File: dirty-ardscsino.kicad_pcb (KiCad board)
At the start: 2 copper layers, 42.7 x 75.2 mm, 15 parts, among them J1 SCSI, J2 Ext. Power (Unused), J3 DM3AT-SF-PEJM5, U1 STM32 Bluepill

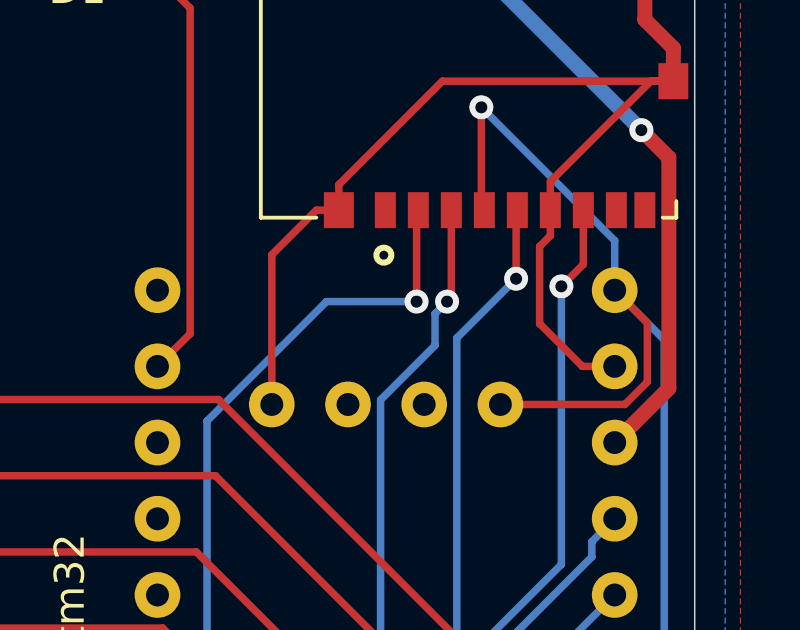
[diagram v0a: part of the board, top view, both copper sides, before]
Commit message: Delete programming header from bluepill footprint
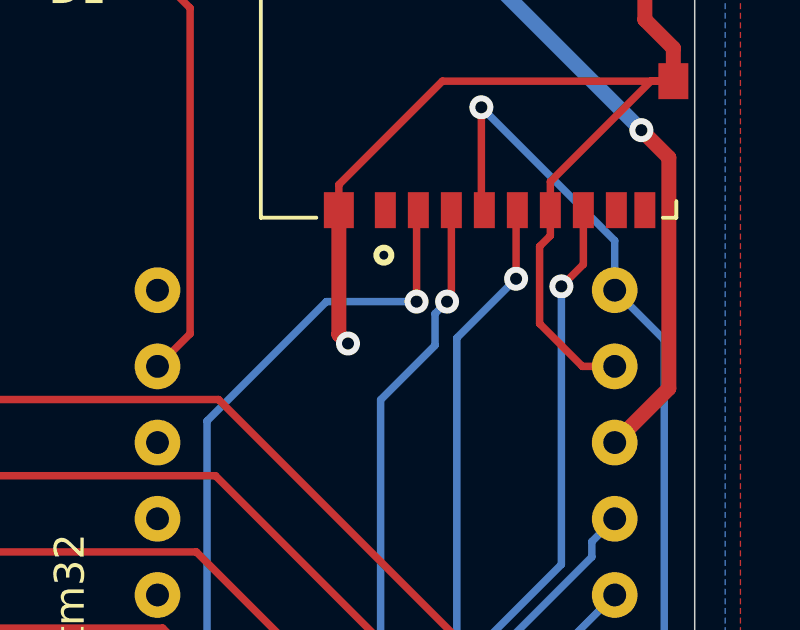
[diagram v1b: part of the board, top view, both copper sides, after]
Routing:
- net /SD_VCC: track 85.3 -> 76.6 mm
- net GND: track 88.5 -> 85.2 mm, vias 2 -> 3
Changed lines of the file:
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@@
     (thickness 1.6)
     (drawings 10)
-    (tracks 341)
+    (tracks 337)
     (zones 0)
     (modules 15)
-    (nets 50)
+    (nets 48)
   )
   (page A4)
@@
   (net 42 "Net-(U1-PadPC14)")
   (net 43 "Net-(U1-PadNRST)")
-  (net 44 "Net-(U1-PadPB2)")
-  (net 45 "Net-(U1-PadBOOT)")
-  (net 46 "Net-(J3-PadSWA)")
-  (net 47 "Net-(J3-PadSWB)")
-  (net 48 "Net-(J3-Pad8)")
-  (net 49 "Net-(J3-Pad1)")
+  (net 44 "Net-(J3-PadSWA)")
+  (net 45 "Net-(J3-PadSWB)")
+  (net 46 "Net-(J3-Pad8)")
+  (net 47 "Net-(J3-Pad1)")
   (net_class Default "This is the default net class."
     (clearance 0.2)
@@
     (add_net "Net-(R2-Pad2)")
     (add_net "Net-(R3-Pad2)")
-    (add_net "Net-(U1-PadBOOT)")
     (add_net "Net-(U1-PadNRST)")
     (add_net "Net-(U1-PadPA0)")
@@
     (add_net "Net-(U1-PadPA3)")
     (add_net "Net-(U1-PadPB1)")
-    (add_net "Net-(U1-PadPB2)")
     (add_net "Net-(U1-PadPC14)")
     (add_net "Net-(U1-PadPC15)")
@@
     (pad PB11 thru_hole circle (at 5.715 -10.795 180) (size 1.524 1.524) (drill 0.762) (layers *.Cu *.Mask)
       (net 21 /SCSI_DAT3))
-    (pad PB2 smd circle (at 2.54 27.305 180) (size 1.524 1.524) (layers Dwgs.User)
-      (net 44 "Net-(U1-PadPB2)"))
-    (pad BOOT smd circle (at 2.54 25.4 180) (size 1.524 1.524) (layers Dwgs.User)
-      (net 45 "Net-(U1-PadBOOT)"))
-    (pad 3V3 thru_hole circle (at -5.715 23.495 180) (size 1.524 1.524) (drill 0.762) (layers *.Cu *.Mask)
-      (net 3 /SD_VCC))
-    (pad SWO thru_hole circle (at -3.175 23.495 180) (size 1.524 1.524) (drill 0.762) (layers *.Cu *.Mask))
-    (pad SWCLK thru_hole circle (at -0.635 23.495 180) (size 1.524 1.524) (drill 0.762) (layers *.Cu *.Mask))
-    (pad G thru_hole circle (at 1.905 23.495 180) (size 1.524 1.524) (drill 0.762) (layers *.Cu *.Mask)
-      (net 2 GND))
   )
   (module Symbol:OSHW-Logo2_14.6x12mm_SilkScreen locked (layer B.Cu)
@@
       (effects (font (size 1 1) (thickness 0.15)))
     )
+    (fp_circle (center 0 0) (end 3.45 0) (layer F.CrtYd) (width 0.05))
+    (fp_circle (center 0 0) (end 3.2 0) (layer Cmts.User) (width 0.15))
     (fp_text user %R (at 0.3 0) (layer F.Fab)
       (effects (font (size 1 1) (thickness 0.15)))
     )
-    (fp_circle (center 0 0) (end 3.2 0) (layer Cmts.User) (width 0.15))
-    (fp_circle (center 0 0) (end 3.45 0) (layer F.CrtYd) (width 0.05))
     (pad 1 np_thru_hole circle (at 0 0) (size 3.2 3.2) (drill 3.2) (layers *.Cu *.Mask))
   )
@@
       (net 2 GND))
     (pad SWA smd rect (at -6.4 10.5 180) (size 1 0.8) (layers F.Cu F.Paste F.Mask)
-      (net 46 "Net-(J3-PadSWA)"))
+      (net 44 "Net-(J3-PadSWA)"))
     (pad P1 smd rect (at -6.4 4.3 180) (size 1 1.2) (layers F.Cu F.Paste F.Mask)
       (net 2 GND))
@@
       (net 2 GND))
     (pad SWB smd rect (at -5.45 0 180) (size 0.7 1.2) (layers F.Cu F.Paste F.Mask)
-      (net 47 "Net-(J3-PadSWB)"))
+      (net 45 "Net-(J3-PadSWB)"))
     (pad 8 smd rect (at -4.5 0 180) (size 0.7 1.2) (layers F.Cu F.Paste F.Mask)
-      (net 48 "Net-(J3-Pad8)"))
+      (net 46 "Net-(J3-Pad8)"))
     (pad 7 smd rect (at -3.4 0 180) (size 0.7 1.2) (layers F.Cu F.Paste F.Mask)
       (net 33 /SD_MISO))
@@
       (net 39 /SD_CS))
     (pad 1 smd rect (at 3.2 0 180) (size 0.7 1.2) (layers F.Cu F.Paste F.Mask)
-      (net 49 "Net-(J3-Pad1)"))
+      (net 47 "Net-(J3-Pad1)"))
   )
   (module Resistor_THT:R_Array_SIP10 (layer F.Cu)
@@
   (segment (start 175.922001 98.397999) (end 175.922001 90.705001) (width 0.5) (layer F.Cu) (net 1))
   (segment (start 175.922001 90.705001) (end 175.006 89.789) (width 0.5) (layer F.Cu) (net 1))
-  (segment (start 174.117 100.203) (end 175.922001 98.397999) (width 0.5) (layer F.Cu) (net 1))
-  (segment (start 163.195 77.978) (end 155.194 77.978) (width 0.5) (layer B.Cu) (net 1))
+  (segment (start 174.117 100.203) (end 175.922001 98.397999) (width 0.5) (layer F.Cu) (net 1) (status 10))
+  (segment (start 163.195 77.978) (end 155.194 77.978) (width 0.5) (layer B.Cu) (net 1) (status 20))
   (segment (start 175.006 89.789) (end 163.195 77.978) (width 0.5) (layer B.Cu) (net 1))
   (segment (start 163.022 77.806) (end 162.572 77.356) (width 0.5) (layer F.Cu) (net 2) (status 30))
@@
   (segment (start 146.304 89.154) (end 146.558 88.9) (width 0.5) (layer F.Cu) (net 2))
   (segment (start 146.304 90.914) (end 146.304 89.154) (width 0.5) (layer F.Cu) (net 2) (status 10))
-  (segment (start 164.172 92.456) (end 164.922 92.456) (width 0.25) (layer F.Cu) (net 2) (status 20))
-  (segment (start 162.687 93.941) (end 164.172 92.456) (width 0.25) (layer F.Cu) (net 2))
-  (segment (start 162.687 98.933) (end 162.687 93.941) (width 0.25) (layer F.Cu) (net 2) (status 10))
   (segment (start 157.79937 140.843) (end 158.877 140.843) (width 0.25) (layer B.Cu) (net 2) (status 20))
   (segment (start 157.506369 140.549999) (end 157.79937 140.843) (width 0.25) (layer B.Cu) (net 2))
@@
   (via (at 162.814 79.375) (size 0.8) (drill 0.4) (layers F.Cu B.Cu) (net 2))
   (segment (start 162.572 79.133) (end 162.814 79.375) (width 0.25) (layer F.Cu) (net 2))
-  (segment (start 162.572 77.356) (end 162.572 79.133) (width 0.25) (layer F.Cu) (net 2))
+  (segment (start 162.572 77.356) (end 162.572 79.133) (width 0.25) (layer F.Cu) (net 2) (status 10))
+  (via (at 165.227 96.901) (size 0.8) (drill 0.4) (layers F.Cu B.Cu) (net 2))
+  (segment (start 164.922 96.596) (end 165.227 96.901) (width 0.5) (layer F.Cu) (net 2))
+  (segment (start 164.922 92.456) (end 164.922 96.596) (width 0.5) (layer F.Cu) (net 2))
   (segment (start 174.638761 141.930001) (end 175.768 140.800762) (width 0.25) (layer B.Cu) (net 3))
   (segment (start 169.968238 138.303) (end 173.595239 141.930001) (width 0.25) (layer B.Cu) (net 3))
@@
   (segment (start 175.768 96.774) (end 174.117 95.123) (width 0.25) (layer B.Cu) (net 3) (status 20))
   (segment (start 175.768 140.800762) (end 175.768 96.774) (width 0.25) (layer B.Cu) (net 3))
-  (segment (start 175.204001 96.210001) (end 174.117 95.123) (width 0.25) (layer F.Cu) (net 3) (status 20))
-  (segment (start 175.204001 98.184761) (end 175.204001 96.210001) (width 0.25) (layer F.Cu) (net 3))
-  (segment (start 174.455762 98.933) (end 175.204001 98.184761) (width 0.25) (layer F.Cu) (net 3))
-  (segment (start 170.307 98.933) (end 174.455762 98.933) (width 0.25) (layer F.Cu) (net 3) (status 10))
   (segment (start 174.117 93.472) (end 169.672 89.027) (width 0.25) (layer B.Cu) (net 3))
   (via (at 169.672 89.027) (size 0.8) (drill 0.4) (layers F.Cu B.Cu) (net 3))
@@
   (segment (start 151.675999 103.848001) (end 160.171811 103.848001) (width 0.25) (layer F.Cu) (net 8))
   (segment (start 150.876 104.648) (end 151.675999 103.848001) (width 0.25) (layer F.Cu) (net 8) (status 10))
-  (segment (start 144.272 112.268) (end 150.876 112.268) (width 0.25) (layer F.Cu) (net 11) (status 30))
   (segment (start 144.272 107.188) (end 150.876 107.188) (width 0.25) (layer F.Cu) (net 9) (status 30))
   (segment (start 143.472001 106.388001) (end 144.272 107.188) (width 0.25) (layer F.Cu) (net 9) (status 20))
@@
   (segment (start 168.105762 115.443) (end 159.050763 106.388001) (width 0.25) (layer F.Cu) (net 9))
   (segment (start 174.117 115.443) (end 168.105762 115.443) (width 0.25) (layer F.Cu) (net 9) (status 10))
-  (segment (start 144.272 114.808) (end 150.876 114.808) (width 0.25) (layer F.Cu) (net 12) (status 30))
-  (segment (start 144.272 117.348) (end 150.876 117.348) (width 0.25) (layer F.Cu) (net 13) (status 30))
   (segment (start 150.876 109.728) (end 144.272 109.728) (width 0.25) (layer F.Cu) (net 10) (status 30))
   (segment (start 141.325012 93.229599) (end 140.875001 92.779589) (width 0.25) (layer F.Cu) (net 10))
@@
   (segment (start 168.783 117.983) (end 174.117 117.983) (width 0.25) (layer F.Cu) (net 10) (status 20))
   (segment (start 159.728001 108.928001) (end 168.783 117.983) (width 0.25) (layer F.Cu) (net 10))
+  (segment (start 144.272 112.268) (end 150.876 112.268) (width 0.25) (layer F.Cu) (net 11) (status 30))
   (segment (start 141.325012 105.293188) (end 142.225034 106.19321) (width 0.25) (layer F.Cu) (net 11))
   (segment (start 138.335001 92.804999) (end 140.264001 92.804999) (width 0.25) (layer F.Cu) (net 11))
@@
   (segment (start 169.545 120.523) (end 174.117 120.523) (width 0.25) (layer F.Cu) (net 11) (status 20))
   (segment (start 160.490001 111.468001) (end 169.545 120.523) (width 0.25) (layer F.Cu) (net 11))
+  (segment (start 144.272 114.808) (end 150.876 114.808) (width 0.25) (layer F.Cu) (net 12) (status 30))
   (segment (start 140.238591 100.399589) (end 140.875001 101.035999) (width 0.25) (layer F.Cu) (net 12))
   (segment (start 141.775023 106.379611) (end 141.775023 112.311023) (width 0.25) (layer F.Cu) (net 12))
@@
   (segment (start 150.876 114.808) (end 152.00737 114.808) (width 0.25) (layer F.Cu) (net 12) (status 10))
   (segment (start 173.736 127.762) (end 174.117 128.143) (width 0.25) (layer F.Cu) (net 12) (status 30))
+  (segment (start 144.272 117.348) (end 150.876 117.348) (width 0.25) (layer F.Cu) (net 13) (status 30))
   (segment (start 138.524999 104.868589) (end 139.161409 105.504999) (width 0.25) (layer F.Cu) (net 13))
   (segment (start 137.16 99.06) (end 137.16 99.860998) (width 0.25) (layer F.Cu) (net 13) (status 30))

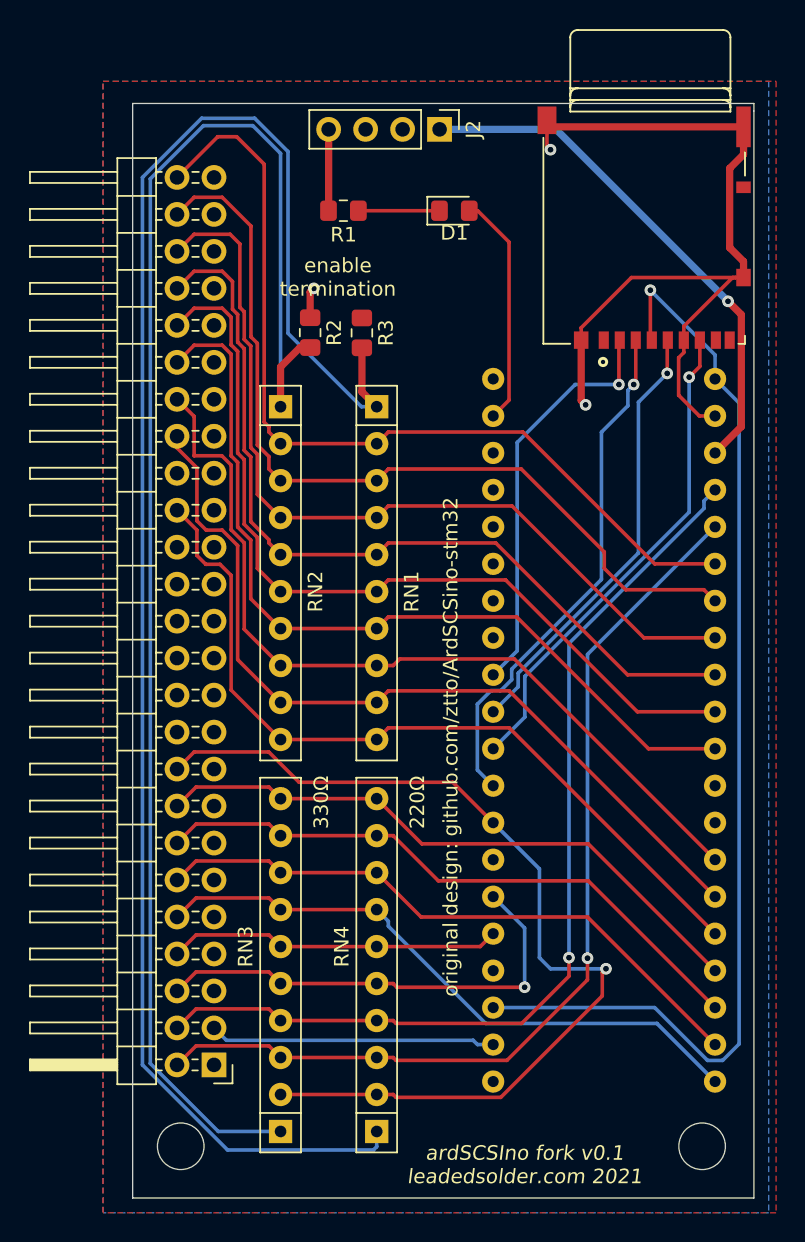
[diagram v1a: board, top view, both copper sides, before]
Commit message: Add shore power switch and decoupling
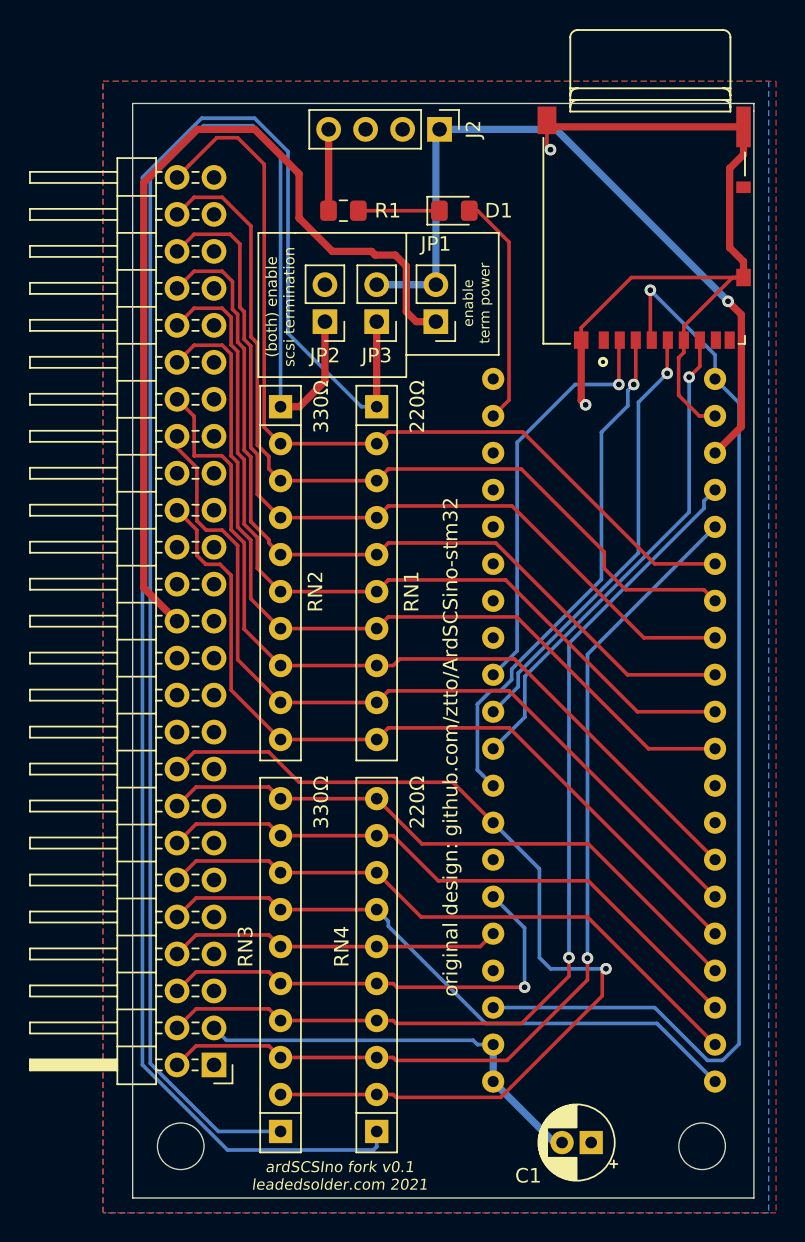
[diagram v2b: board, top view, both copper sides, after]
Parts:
- removed R2, R3: 0Ω, Resistor_SMD:R_0805_2012Metric_Pad1.15x1.40mm_HandSolder
- added C1: 4.7µF, Capacitor_THT:CP_Radial_D5.0mm_P2.00mm, F.Cu at (165.6, 147.6)
- added JP1: Jumper_NC_Small, Connector_PinHeader_2.54mm:PinHeader_1x02_P2.54mm_Vertical, F.Cu at (154.9, 91.2)
- added JP2: Term_Enable_PD, Connector_PinHeader_2.54mm:PinHeader_1x02_P2.54mm_Vertical, F.Cu at (147.3, 91.2)
- added JP3: Term_Enable_PU, Connector_PinHeader_2.54mm:PinHeader_1x02_P2.54mm_Vertical, F.Cu at (150.9, 91.2)
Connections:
- J2 pad 1: /TERM_POWER -> +5V
- U1 pad 5V: /TERM_POWER -> +5V
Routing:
- net +5V: track 0.00 -> 51.1 mm, vias 0 -> 1
- net /TERM_POWER: track 36.2 -> 61.7 mm, vias 1 -> 0
- net GND: track 85.2 -> 92.1 mm, vias 3 -> 2
- net Net-(JP2-Pad1): track 105.6 -> 108.2 mm
- net Net-(JP3-Pad1): track 118.4 -> 119.7 mm
- added copper zone on F.Cu, net +5V
- removed copper zone on F.Cu, net /TERM_POWER
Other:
- board text added: "(both) enable scsi termination"
- board text added: "3v3"
- board text added: "5v"
- board text added: "ACK"
- board text added: "ATN"
- board text added: "Busy"
- board text added: "CD"
- board text added: "DBP"
- board text added: "Data 0"
- board text added: "Data 1"
- board text added: "Data 2"
- board text added: "Data 3"
- board text added: "Data 4"
- board text added: "Data 5"
- board text added: "Data 6"
- board text added: "Data 7"
- board text added: "GND"
- board text added: "I/O"
- board text added: "MSG"
- board text added: "REQ"
- board text added: "Reset"
- board text added: "SEL"
- board text added: "Term. Power"
- board text added: "enable term power"
- board text removed: "enable termination"

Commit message: Clean up silks
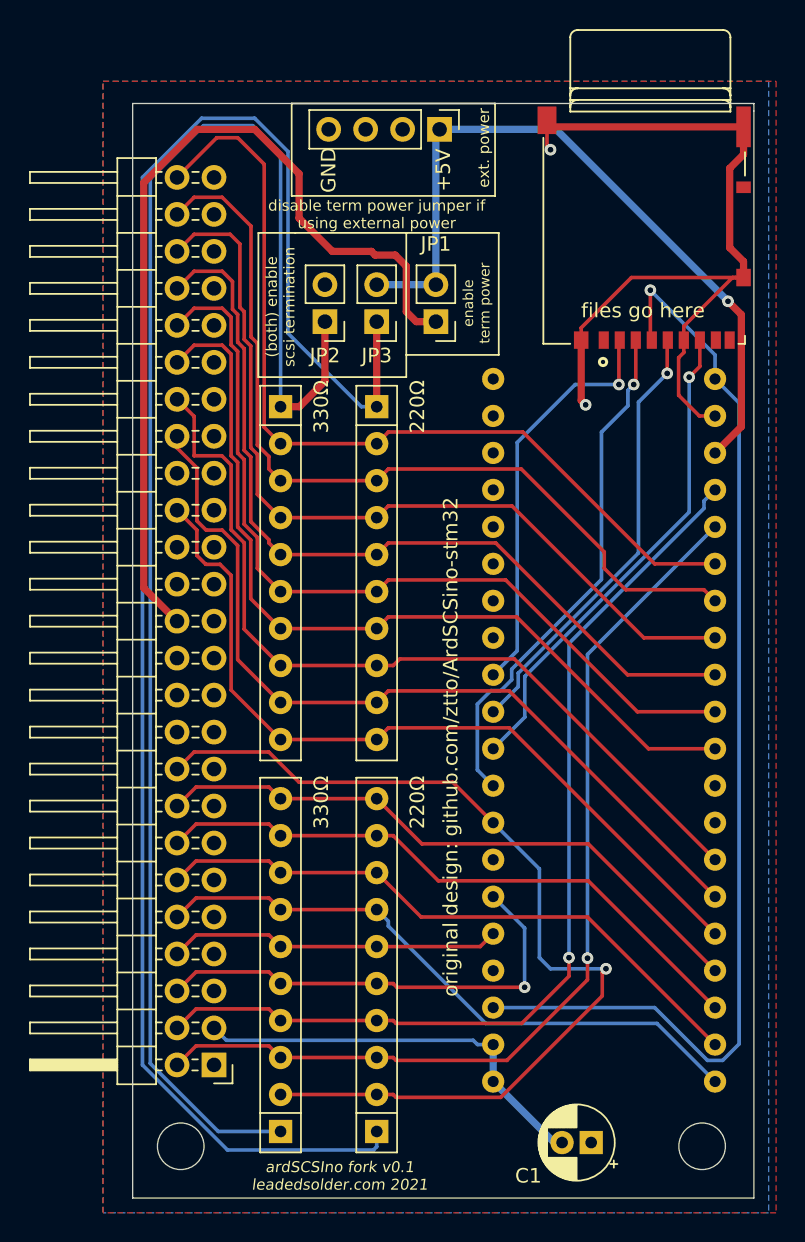
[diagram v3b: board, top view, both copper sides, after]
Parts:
- removed D1: LED, LED_SMD:LED_0805_2012Metric_Pad1.15x1.40mm_HandSolder
- removed R1: 75Ω, Resistor_SMD:R_0805_2012Metric_Pad1.15x1.40mm_HandSolder
- JP2: value Term_Enable_PD -> Jumper_NC_Small
- JP3: value Term_Enable_PU -> Jumper_NC_Small
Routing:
- net Net-(U1-PadPC13): track 16.0 -> 0.00 mm
- net GND: track 92.1 -> 86.5 mm
- net Net-(D1-Pad1): track 5.57 -> 0.00 mm
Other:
- board text added: "+5V"
- board text added: "disable term power jumper if using external power"
- board text added: "ext. power"
- board text added: "files go here"
